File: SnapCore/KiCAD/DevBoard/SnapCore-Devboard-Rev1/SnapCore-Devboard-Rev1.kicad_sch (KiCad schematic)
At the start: 58 parts, among them J2 USB_C_Receptacle_USB2.0_16P, J3 Conn_01x18_Pin, Q1 AO3407A, SW2 TS-1187A, U1 nRF52840-QIXX, U2 XC6220B331MR, U5 TP4056-42-ESOP8, Y1 32.768KHz, Y2 32MHz

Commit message: Updated Devboard to use Chip Antenna instead of PCB Antenna for easier RF matching
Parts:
- removed AE1: SWRA117D_2.4Ghz, RF_Antenna:Texas_SWRA117D_2.4GHz_Right, symbol Device:Antenna_Chip
- removed C17: 1nF, Capacitor_SMD:C_0402_1005Metric, symbol Device:C
- removed R7: 0R, Resistor_SMD:R_0603_1608Metric, symbol Device:R
- added AE2: AMCA31-2R450G-S1F-T3, AMCA31-2R450G-S1F-T3:XDCR_AMCA31-2R450G-S1F-T3, symbol Device:Antenna
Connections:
- net at C16.1, L1.2: now also AE2.1 (A)

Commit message: Switched to TP4057 Charger IC, Added J4 to bottom pinout
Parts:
- removed BAT_CONN2: Battery JST 3.7V, Connector_JST:JST_EH_B2B-EH-A_1x02_P2.50mm_Vertical, symbol Connector:Conn_01x02_Pin
- removed C2, C24: 10uF, Capacitor_SMD:C_0402_1005Metric, symbol Device:C
- removed C23: 2.2uF, Capacitor_SMD:C_0805_2012Metric, symbol Device:C
- removed D1: Red, LED_SMD:LED_0805_2012Metric, symbol Device:LED
- removed D2: Green, LED_SMD:LED_0805_2012Metric, symbol Device:LED
- removed F2: 500mA, Fuse:Fuse_1206_3216Metric, symbol Device:Fuse_Small
- removed R22: 1M_1%, Resistor_SMD:R_0603_1608Metric, symbol Device:R
- removed R23: 510k_1%, Resistor_SMD:R_0603_1608Metric, symbol Device:R
- removed R3, R4: 1k, Resistor_SMD:R_0603_1608Metric, symbol Device:R
- removed R5: 4k, Resistor_SMD:R_0603_1608Metric, symbol Device:R
- removed U5: TP4056-42-ESOP8, Package_SO:SOIC-8-1EP_3.9x4.9mm_P1.27mm_EP2.41x3.3mm_ThermalVias, symbol Battery_Management:TP4056-42-ESOP8
- added BAT_CONN1: Battery JST 3.7V, Connector_JST:JST_EH_B2B-EH-A_1x02_P2.50mm_Vertical, symbol Connector:Conn_01x02_Pin
- added C4: 2.2uF, Capacitor_SMD:C_0805_2012Metric, symbol Device:C
- added C5: 10uF, Capacitor_SMD:C_0402_1005Metric, symbol Device:C
- added C6: 2.2uF, Capacitor_SMD:C_0603_1608Metric, symbol Device:C
- added D3: Green, LED_SMD:LED_0805_2012Metric, symbol Device:LED
- added D4: Red, LED_SMD:LED_0805_2012Metric, symbol Device:LED
- added F1: 500mA, Fuse:Fuse_1206_3216Metric, symbol Device:Fuse_Small
- added R10: 1M_1%, Resistor_SMD:R_0603_1608Metric, symbol Device:R
- added R11: 510k_1%, Resistor_SMD:R_0603_1608Metric, symbol Device:R
- added R7: 330R, Resistor_SMD:R_0603_1608Metric, symbol Device:R
- added R8: 4k, Resistor_SMD:R_0603_1608Metric, symbol Device:R
- added TP1: VBUS, TestPoint:TestPoint_Pad_D2.0mm, symbol Connector:TestPoint
- added TP2: VBAT, TestPoint:TestPoint_Pad_D2.0mm, symbol Connector:TestPoint
- added TP3: 3V3, TestPoint:TestPoint_Pad_D2.0mm, symbol Connector:TestPoint
- added TP4: GND, TestPoint:TestPoint_Pad_D2.0mm, symbol Connector:TestPoint
- added TP5: RESET, TestPoint:TestPoint_Pad_D2.0mm, symbol Connector:TestPoint
- added TP6: RF, TestPoint:TestPoint_Pad_D2.0mm, symbol Connector:TestPoint
- added TP7: PROG, TestPoint:TestPoint_Pad_D2.0mm, symbol Connector:TestPoint
- added U4: TP4057, Package_TO_SOT_SMD:TSOT-23-6, symbol Battery_Management:TP4057
- C7: value 100NF -> 100nF
- Y1: footprint Crystal:Crystal_SMD_2016-4Pin_2.0x1.6mm -> Crystal:Crystal_SMD_3215-2Pin_3.2x1.5mm
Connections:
- net 3V3: now also TP3.1
- net ANT_H23: now also TP6.1
- net BAT0: now also C4.1, C5.1, F1.2, R10.1, TP2.1, U4.3 (BAT)
- net GND: now also BAT_CONN1.2 (Pin_2), C4.2, C5.2, C6.1, R8.2, TP4.1, U4.2 (GND); no longer J3.18 (Pin_18)
- net P0.04_AIN2_A4_D4: now also J3.18 (Pin_18)
- net P0.14_READ_BAT: now also R11.1
- net P0.31_AIN7_BAT: now also R10.2, R11.2
- net RESET: now also TP5.1
- net VBUS: now also C6.2, R7.1, TP1.1, U4.4 (V_{CC})
- new net: BAT_CONN1.1 (Pin_1), F1.1
- new net: D4.1 (K), U4.1 (~{CHRG})
- new net: D3.1 (K), U4.5 (STDBY)
- new net: R8.1, TP7.1, U4.6 (PROG)
- new net: D3.2 (A), D4.2 (A), R7.2

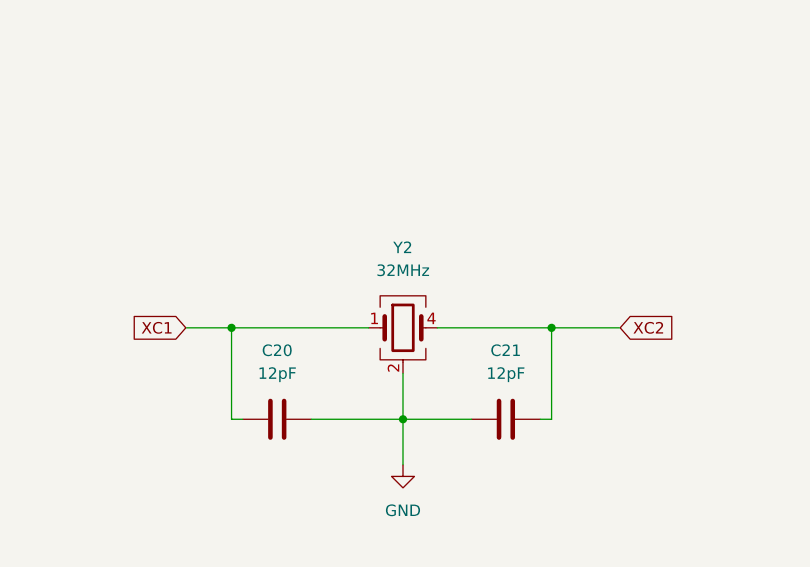
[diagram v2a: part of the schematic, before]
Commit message: Final Rev1 fix before ordering
Fixed Y2 not having correct pinout
Made pcb antenna smaller to have it closer to the edge of the board
Final routing adjustments
Adjusted RF matching circuit
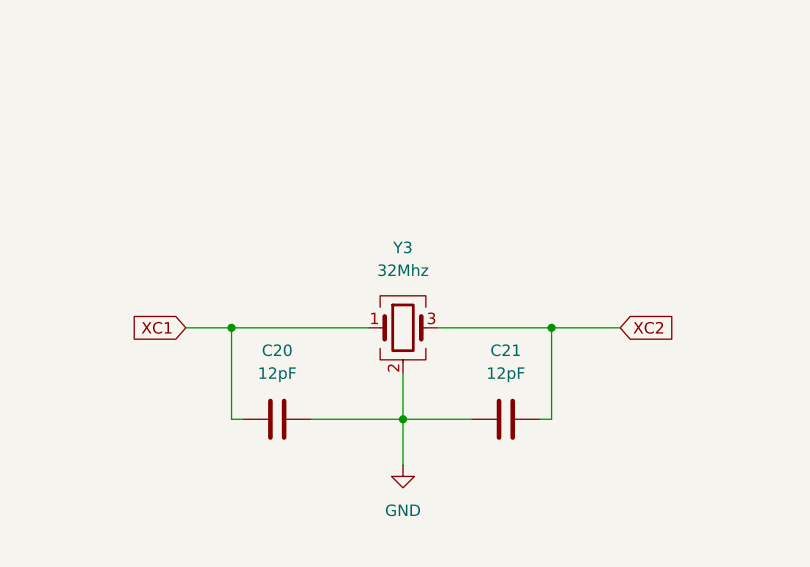
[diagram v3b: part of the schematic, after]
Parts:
- removed Y2: 32MHz, Crystal:Crystal_SMD_2016-4Pin_2.0x1.6mm, symbol Device:Crystal_GND23
- added Y3: 32Mhz, Crystal:Crystal_SMD_2016-4Pin_2.0x1.6mm, symbol Device:Crystal_GND24
- BAT_CONN1: footprint Connector_JST:JST_EH_B2B-EH-A_1x02_P2.50mm_Vertical -> Connector_JST:JST_PH_B2B-PH-K_1x02_P2.00mm_Vertical
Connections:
- net GND: now also Y3.2 (G), Y3.4 (G)
- net XC1: now also Y3.1
- net XC2: now also Y3.3
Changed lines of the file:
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@@
 			)
 		)
-		(property "Footprint" "Connector_JST:JST_EH_B2B-EH-A_1x02_P2.50mm_Vertical"
+		(property "Footprint" "Connector_JST:JST_PH_B2B-PH-K_1x02_P2.00mm_Vertical"
 			(at 496.57 102.87 0)
 			(effects
@@
 	)
 	(symbol
-		(lib_id "Device:Crystal_GND23")
-		(at 77.47 80.01 0)
-		(unit 1)
-		(exclude_from_sim no)
-		(in_bom yes)
-		(on_board yes)
-		(dnp no)
-		(fields_autoplaced yes)
-		(property "Reference" "Y2"
-			(at 77.47 71.12 0)
-			(effects
-				(font
-					(size 1.27 1.27)
-				)
-			)
-		)
-		(property "Value" "32MHz"
-			(at 77.47 73.66 0)
-			(effects
-				(font
-					(size 1.27 1.27)
-				)
-			)
-		)
-		(property "Footprint" "Crystal:Crystal_SMD_2016-4Pin_2.0x1.6mm"
-			(at 77.47 80.01 0)
-			(effects
-				(font
-					(size 1.27 1.27)
-				)
-				(hide yes)
-			)
-		)
-		(property "Datasheet" "~"
-			(at 77.47 80.01 0)
-			(effects
-				(font
-					(size 1.27 1.27)
-				)
-				(hide yes)
-			)
-		)
-		(property "Description" "Four pin crystal, GND on pins 2 and 3"
-			(at 77.47 80.01 0)
-			(effects
-				(font
-					(size 1.27 1.27)
-				)
-				(hide yes)
-			)
-		)
-		(property private "KLC_S3.3" "The rectangle is not a symbol body but a graphical element"
-			(at 77.47 92.71 0)
-			(show_name yes)
-			(effects
-				(font
-					(size 1.27 1.27)
-				)
-				(hide yes)
-			)
-		)
-		(property private "KLC_S4.1" "Some pins are on 50mil grid to make the symbol small"
-			(at 77.47 95.25 0)
-			(show_name yes)
-			(effects
-				(font
-					(size 1.27 1.27)
-				)
-				(hide yes)
-			)
-		)
-		(pin "3"
-		)
-		(pin "1"
-		)
-		(pin "4"
-		)
-		(pin "2"
-		)
-		(instances
-			(project ""
-				(path "/f0abf294-ed6a-491b-abc8-f6e6594dbb09"
-					(reference "Y2")
-					(unit 1)
-				)
-			)
-		)
-	)
-	(symbol
 		(lib_id "Connector:TestPoint")
 		(at 228.6 132.08 0)
@@
 					(unit 1)
 				)
+			)
+		)
+	)
+	(symbol
+		(lib_id "Device:Crystal_GND24")
+		(at 77.47 80.01 0)
+		(unit 1)
+		(exclude_from_sim no)
+		(in_bom yes)
+		(on_board yes)
+		(dnp no)
+		(fields_autoplaced yes)
+		(property "Reference" "Y3"
+			(at 77.47 71.12 0)
+			(effects
+				(font
+					(size 1.27 1.27)
+				)
+			)
+		)
+		(property "Value" "32Mhz"
+			(at 77.47 73.66 0)
+			(effects
+				(font
+					(size 1.27 1.27)
+				)
+			)
+		)
+		(property "Footprint" "Crystal:Crystal_SMD_2016-4Pin_2.0x1.6mm"
+			(at 77.47 80.01 0)
+			(effects
+				(font
+					(size 1.27 1.27)
+				)
+				(hide yes)
+			)
+		)
+		(property "Datasheet" "~"
+			(at 77.47 80.01 0)
+			(effects
+				(font
+					(size 1.27 1.27)
+				)
+				(hide yes)
+			)
+		)
+		(property "Description" "Four pin crystal, GND on pins 2 and 4"
+			(at 77.47 80.01 0)
+			(effects
+				(font
+					(size 1.27 1.27)
+				)
+				(hide yes)
+			)
+		)
+		(property private "KLC_S3.3" "The rectangle is not a symbol body but a graphical element"
+			(at 77.47 92.71 0)
+			(show_name yes)
+			(effects
+				(font
+					(size 1.27 1.27)
+				)
+				(hide yes)
+			)
+		)
+		(property private "KLC_S4.1" "Some pins are on 50mil grid to make the symbol small"
+			(at 77.47 95.25 0)
+			(show_name yes)
+			(effects
+				(font
+					(size 1.27 1.27)
+				)
+				(hide yes)
+			)
+		)
+		(pin "2"
+		)
+		(pin "4"
+		)
+		(pin "3"
+		)
+		(pin "1"
+		)
+		(instances
+			(project ""
+				(path "/f0abf294-ed6a-491b-abc8-f6e6594dbb09"
+					(reference "Y3")
+					(unit 1)
+				)
